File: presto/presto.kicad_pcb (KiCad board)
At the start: 2 copper layers, 110 x 110 mm, 60 parts, among them J101 12V IN, J201 Conn_01x03_Pin, J202 Conn_01x03_Pin, J203 Conn_01x03_Pin, J204 Conn_01x03_Pin, J205 Conn_01x03_Pin, J206 Conn_01x03_Pin, J207 Conn_01x03_Pin, J208 Conn_01x03_Pin, J209 Conn_01x03_Pin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

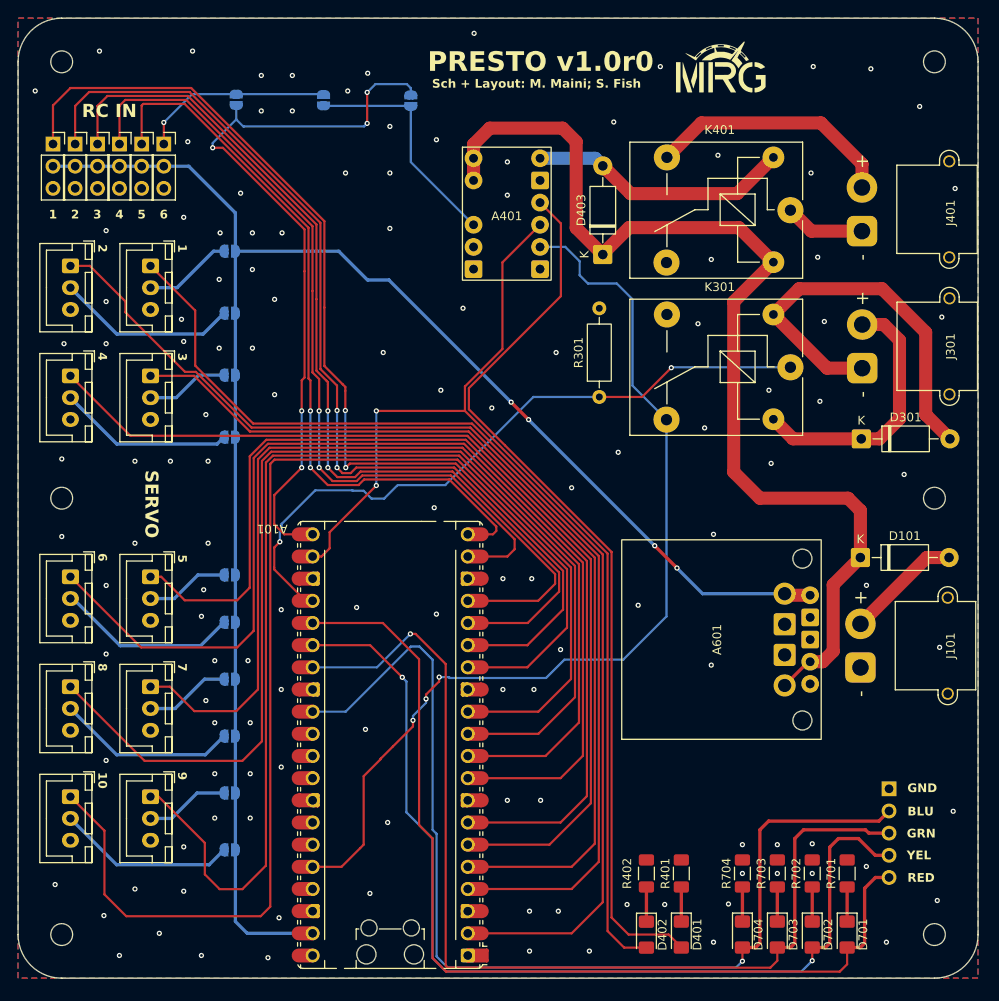
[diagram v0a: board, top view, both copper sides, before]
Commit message: 2-pin JST added for autonomous, 6 routes not connected for some reason though
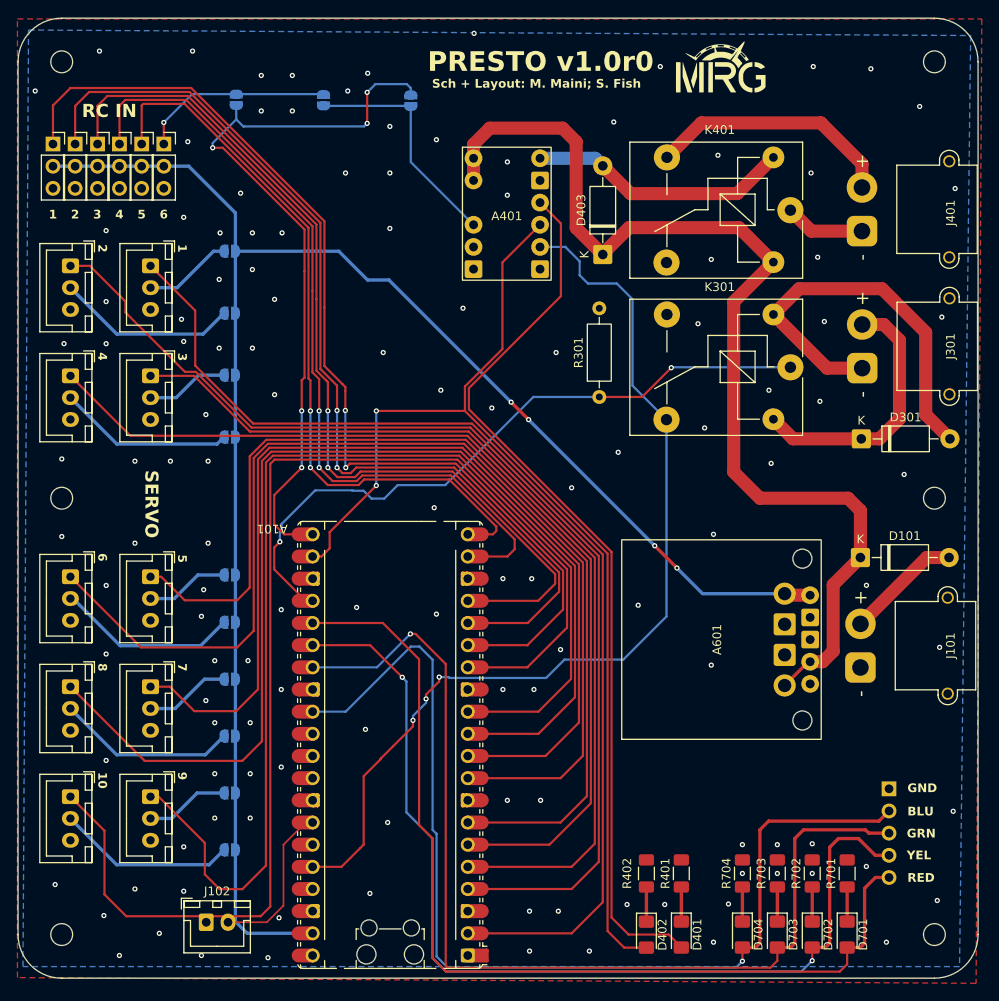
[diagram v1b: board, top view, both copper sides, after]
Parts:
- added J102: Conn_01x02_Pin, Connector_JST:JST_XH_B2B-XH-A_1x02_P2.50mm_Vertical, F.Cu at (96.6, 148.6)
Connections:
- A101 pad 13: GND -> Net-(A101-GND-Pad13)
- A101 pad 18: GND -> Net-(A101-GND-Pad13)
- A101 pad 21: /gpio16 -> unconnected-(A101-GPIO16-Pad21)
- A101 pad 22: /gpio17 -> unconnected-(A101-GPIO17-Pad22)
- A101 pad 23: GND -> Net-(A101-GND-Pad13)
- A101 pad 24: /EStop Reading/estop_signal -> unconnected-(A101-GPIO18-Pad24)
- A101 pad 25: /LED Interface/red -> unconnected-(A101-GPIO19-Pad25)
- A101 pad 26: /LED Interface/yellow -> unconnected-(A101-GPIO20-Pad26)
- A101 pad 27: /LED Interface/green -> unconnected-(A101-GPIO21-Pad27)
- A101 pad 28: GND -> Net-(A101-GND-Pad13)
- A101 pad 29: /LED Interface/blue -> unconnected-(A101-GPIO22-Pad29)
- A101 pad 3: GND -> Net-(A101-GND-Pad13)
- A101 pad 34: unconnected-(A101-GPIO28_ADC2-Pad34)_1 -> Net-(A101-GPIO28_ADC2)
- A101 pad 36: +3V3 -> unconnected-(A101-3V3-Pad36)
- A101 pad 38: GND -> Net-(A101-GND-Pad13)
- A101 pad 39: +5V -> unconnected-(A101-VSYS-Pad39)
- A101 pad 8: GND -> Net-(A101-GND-Pad13)
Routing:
- net Net-(A101-GPIO28_ADC2): track 0.00 -> 17.7 mm
- net Net-(A101-GND-Pad13): track 0.00 -> 2.40 mm
- net GND: track 2.40 -> 0.00 mm

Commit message: added connector for neopixel and fixed autonomy switch layout
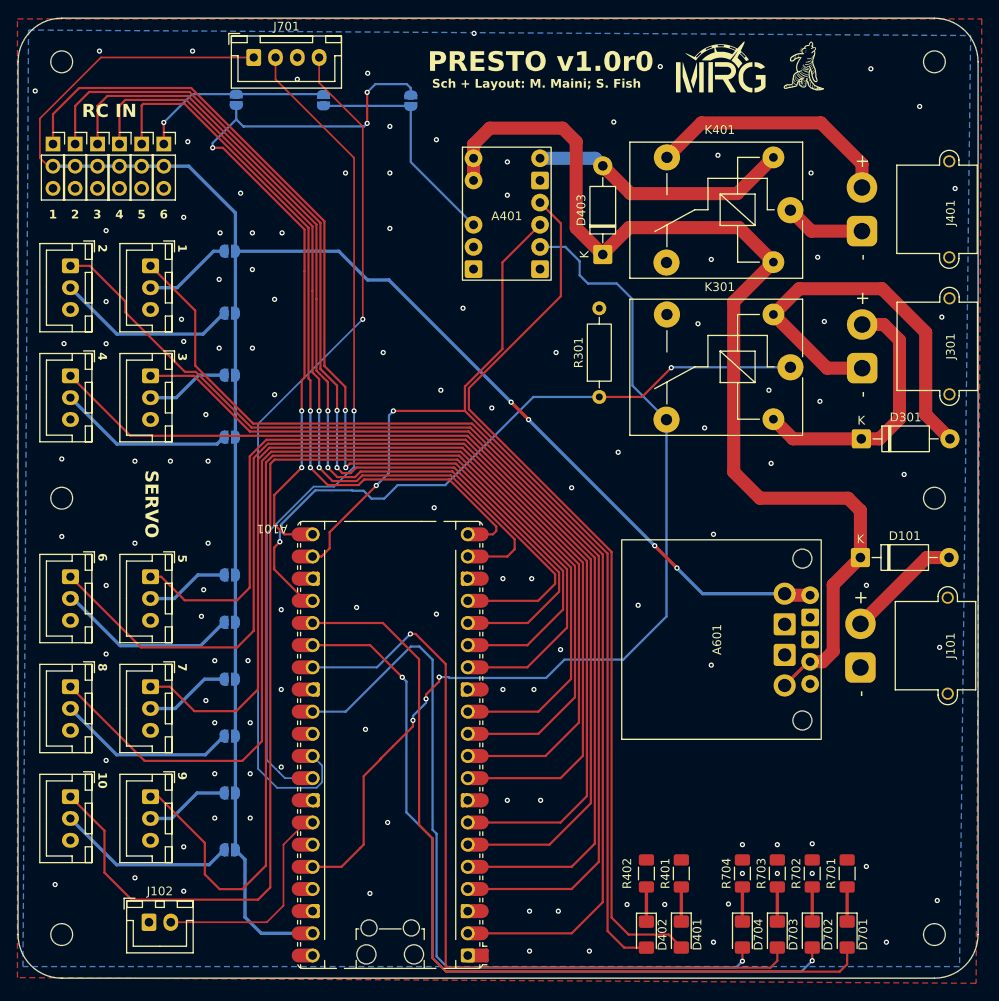
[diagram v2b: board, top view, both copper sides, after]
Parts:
- added G***: LOGO, graphics:victorycat, F.Cu at (165.0, 50.5)
- J701: value LED Connector -> Conn_01x04; footprint Connector_PinSocket_2.54mm:PinSocket_1x05_P2.54mm_Horizontal -> Connector_JST:JST_XH_B4B-XH-A_1x04_P2.50mm_Vertical; moved to F.Cu
- moved J701 111.0 mm to (102.0, 49.5), turned to 0 degrees
- moved J102 6.56 mm to (90.0, 148.6)
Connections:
- A101 pad 13: Net-(A101-GND-Pad13) -> GND
- A101 pad 18: Net-(A101-GND-Pad13) -> GND
- A101 pad 21: unconnected-(A101-GPIO16-Pad21) -> /gpio16
- A101 pad 22: unconnected-(A101-GPIO17-Pad22) -> /gpio17
- A101 pad 23: Net-(A101-GND-Pad13) -> GND
- A101 pad 24: unconnected-(A101-GPIO18-Pad24) -> /EStop Reading/estop_signal
- A101 pad 25: unconnected-(A101-GPIO19-Pad25) -> /LED Interface/red
- A101 pad 26: unconnected-(A101-GPIO20-Pad26) -> /LED Interface/yellow
- A101 pad 27: unconnected-(A101-GPIO21-Pad27) -> /LED Interface/green
- A101 pad 28: Net-(A101-GND-Pad13) -> GND
- A101 pad 29: unconnected-(A101-GPIO22-Pad29) -> /LED Interface/blue
- A101 pad 3: Net-(A101-GND-Pad13) -> GND
- A101 pad 31: unconnected-(A101-GPIO26_ADC0-Pad31) -> /LED Interface/DataIn
- A101 pad 32: unconnected-(A101-GPIO27_ADC1-Pad32) -> /LED Interface/DataOut
- A101 pad 36: unconnected-(A101-3V3-Pad36) -> +3V3
- A101 pad 38: Net-(A101-GND-Pad13) -> GND
- A101 pad 39: unconnected-(A101-VSYS-Pad39) -> +5V
- A101 pad 8: Net-(A101-GND-Pad13) -> GND
- J701 pad 1: GND -> +5V
- J701 pad 2: /LED Interface/blue -> /LED Interface/DataOut
- J701 pad 3: /LED Interface/green -> GND
- J701 pad 4: /LED Interface/yellow -> /LED Interface/DataIn
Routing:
- net /LED Interface/DataIn: track 0.00 -> 100.5 mm, vias 0 -> 1
- net /LED Interface/DataOut: track 0.00 -> 95.9 mm, vias 0 -> 1
- net +5V: track 196.7 -> 229.5 mm
- net /LED Interface/blue: track 120.0 -> 89.1 mm
- net /LED Interface/green: track 118.3 -> 92.8 mm
- net /LED Interface/yellow: track 112.8 -> 91.6 mm
- net /LED Interface/red: track 111.0 -> 99.2 mm
- net Net-(A101-GPIO28_ADC2): track 17.7 -> 24.3 mm
- net /Servo Interface/servo10: track 142.6 -> 138.3 mm
- net Net-(A101-GND-Pad13): track 2.40 -> 0.00 mm
- net GND: track 0.00 -> 2.40 mm, vias 131 -> 119
- net /gpio17: track 127.0 -> 125.8 mm
- net /RC Interface/ch1: track 118.4 -> 117.8 mm
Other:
- board text removed: "BLU"
- board text removed: "GND"
- board text removed: "GRN"
- board text removed: "RED"
- board text removed: "YEL"

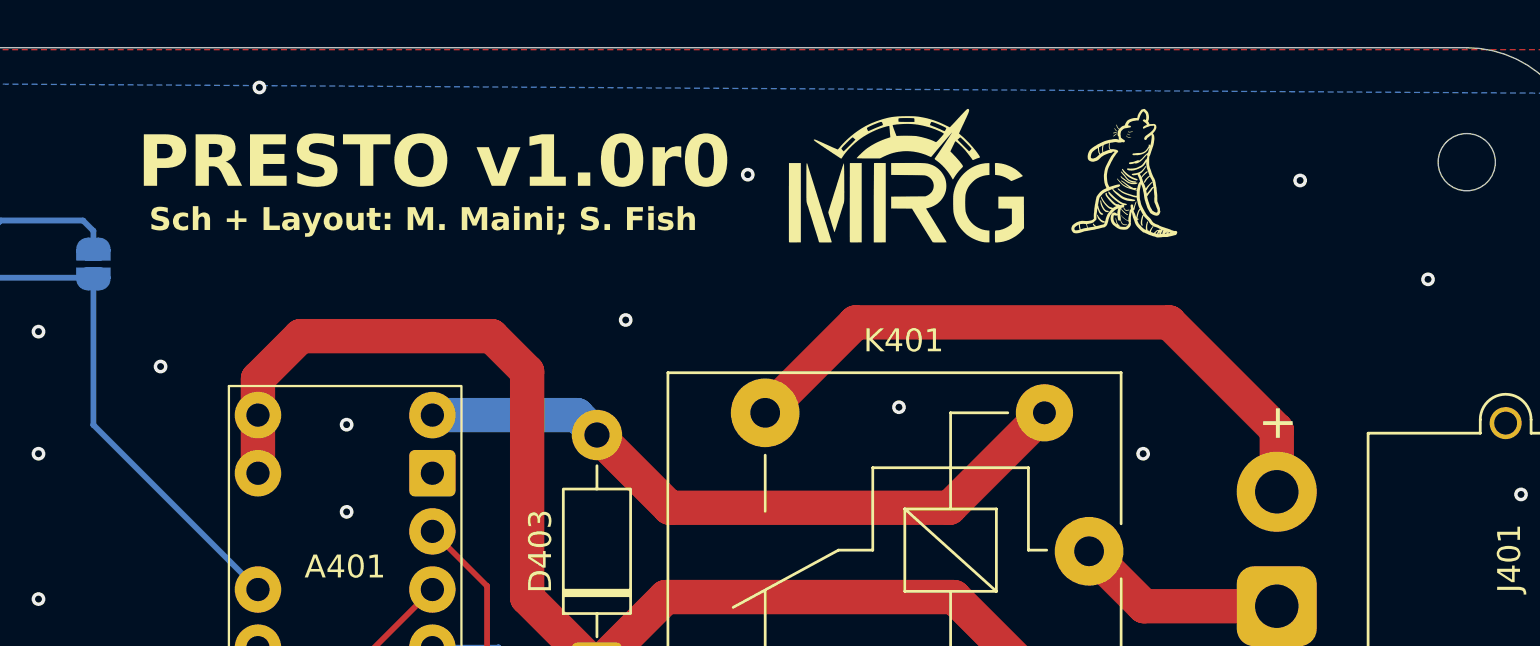
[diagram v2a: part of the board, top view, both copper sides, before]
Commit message: added fuse and changed revision number
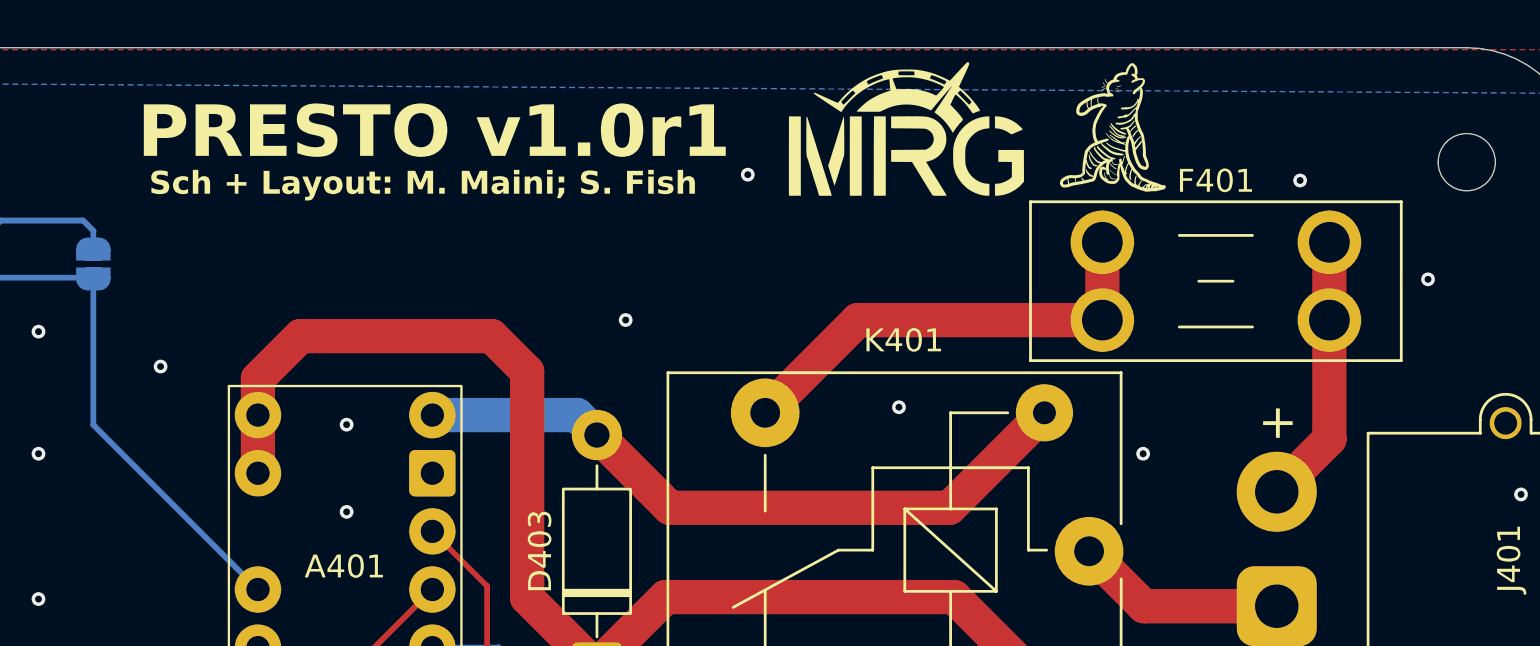
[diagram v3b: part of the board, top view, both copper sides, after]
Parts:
- added F401: Fuse, Fuse:Fuseholder_Blade_Mini_Keystone_3568, F.Cu at (164.1, 53.5)
- moved G*** 2.06 mm to (164.5, 48.5)
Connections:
- K401 pad 3: Net-(J401-Pin_2) -> Net-(F401-Pad1)
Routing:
- net Net-(F401-Pad1): track 0.00 -> 19.8 mm
- net Net-(J401-Pin_2): track 28.6 -> 11.9 mm
- net GND: vias 119 -> 118
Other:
- board text added: "PRESTO v1.0r1"
- board text removed: "PRESTO v1.0r0"
